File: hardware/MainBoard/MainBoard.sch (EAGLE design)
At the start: 238 parts, among them J1 CON-71741-2184-BOT, J2 CON-71741-2184-TOP, J3 CON-FTSH-105-01-L-DV-K, J4 CON-ZX62R-B-5P, J5 CON-SMA, J6 CON-SMA, J7 CON-RJ45-J0G-0007NL, J8 SWITCH-CJS-1200-1200, M1 MOUNT-HOLE3.3, M2 MOUNT-HOLE3.3, M3 MOUNT-HOLE3.3, M4 MOUNT-HOLE3.3, M5 FIDUCIAL1X2, M6 FIDUCIAL1X2, M7 FIDUCIAL1X2, M8 FIDUCIAL1X2, Q1 MMBT3904, SW1 SWITCH-KSC-201J, SW2 SWITCH-KSC-201J, U1 A2F500M3G-FG256, U2 MAX19706-T4877-4, U3 MAX19706-T4877-4, U4 USBLC6-2SC6, U5 FT232HL, U6 DP83848C-VBH48A, U7 93LC56BT-OT, U8 DS1818-10-SOT-23, U9 LMV112, X1 FOX924B, X2 ECX-31B, X3 ASEM1-C, X5 ECX-42-120

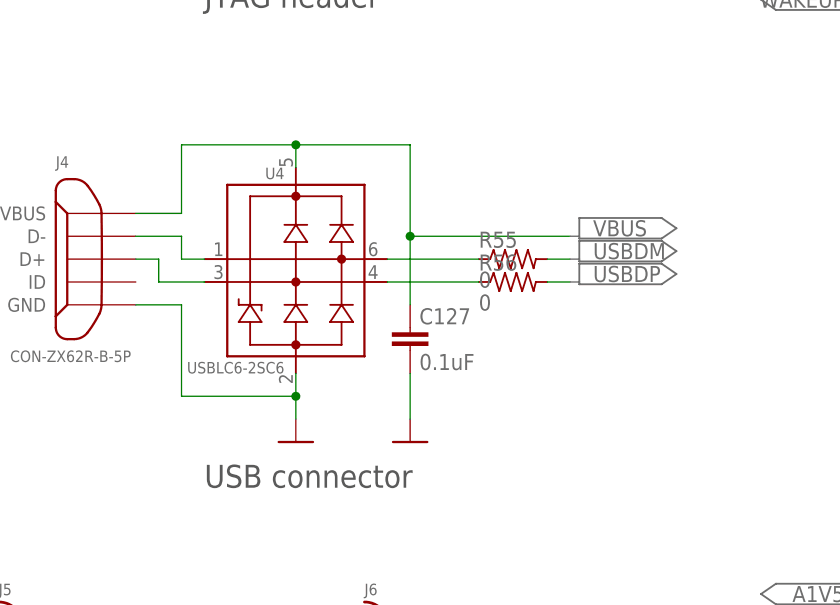
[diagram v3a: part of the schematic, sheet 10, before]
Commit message: Minor corrections in MainBoard library and board.
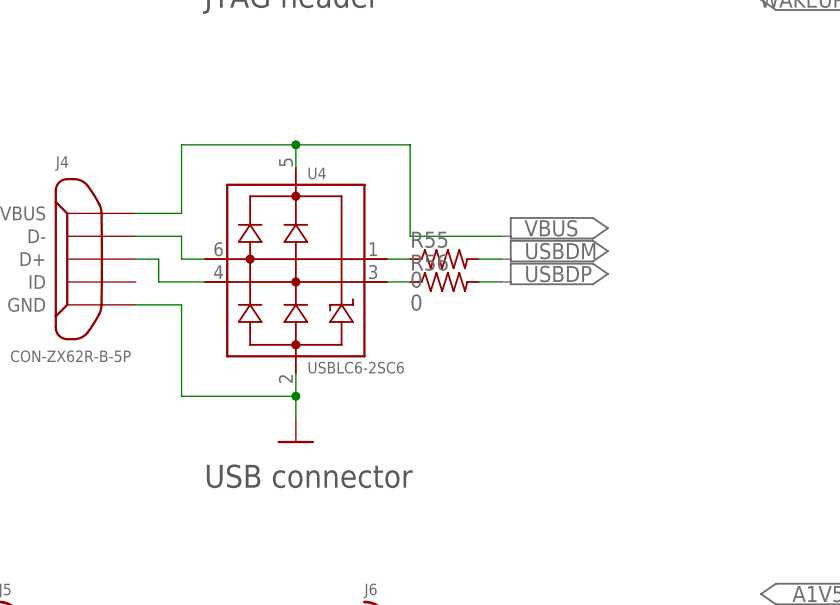
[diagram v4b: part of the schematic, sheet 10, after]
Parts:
- removed C127: 0.1uF, MainBoard:C0402
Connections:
- removed net USBDP-OUT: R56.1, U4.IO2@2
- new net N$26: R56.1, U4.IO2@1
- net DGND: no longer C127.2
- net USBDM-IN: now also U4.IO1@2; no longer U4.IO1@1
- net USBDM-OUT: now also U4.IO1@1; no longer U4.IO1@2
- net USBDP-IN: now also U4.IO2@2; no longer U4.IO2@1
- net VBUS: no longer C127.1
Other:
- note removed: "Place close to USBLC6 output"
- moved on the sheet: R55, R56
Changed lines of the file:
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@@
 <part name="C125" library="MainBoard" deviceset="C" device="0402"/>
 <part name="C126" library="MainBoard" deviceset="C" device="0402"/>
-<part name="C127" library="MainBoard" deviceset="C" device="0402" value="0.1uF"/>
-<part name="U$143" library="MainBoard" deviceset="DGND" device=""/>
 </parts>
 <sheets>
@@
 <instance part="R96" gate="G$1" x="101.6" y="119.38"/>
 <instance part="PORT258" gate="G$1" x="154.94" y="71.12" rot="R90"/>
-<instance part="PORT259" gate="G$1" x="190.5" y="78.74" rot="R90"/>
+<instance part="PORT259" gate="G$1" x="190.5" y="83.82" rot="R90"/>
 <instance part="PORT260" gate="G$1" x="53.34" y="73.66" rot="R90"/>
 <instance part="B2" gate="G$1" x="60.96" y="60.96" rot="R90"/>
@@
 <rectangle x1="60.96" y1="55.88" x2="96.52" y2="68.58" layer="116"/>
 <rectangle x1="17.78" y1="17.78" x2="104.14" y2="30.48" layer="116"/>
-<text x="73.66" y="88.9" size="1.778" layer="150" rot="R90">Place close to USBLC6 output</text>
 </plain>
 <instances>
@@
 <instance part="J6" gate="G1" x="66.04" y="60.96"/>
 <instance part="J4" gate="G$1" x="35.56" y="101.6" rot="MR0"/>
-<instance part="U4" gate="G$1" x="55.88" y="101.6" rot="MR0"/>
+<instance part="U4" gate="G$1" x="55.88" y="101.6"/>
 <instance part="U$13" gate="G$1" x="165.1" y="149.86"/>
 <instance part="PORT15" gate="G$1" x="175.26" y="160.02" rot="MR0"/>
@@
 <instance part="J1" gate="G$1" x="134.62" y="114.3"/>
 <instance part="U$68" gate="G$1" x="55.88" y="81.28"/>
-<instance part="R55" gate="G$1" x="81.28" y="101.6"/>
-<instance part="R56" gate="G$1" x="81.28" y="99.06"/>
-<instance part="PORT172" gate="G$1" x="96.52" y="104.14"/>
-<instance part="PORT173" gate="G$1" x="96.52" y="101.6"/>
-<instance part="PORT174" gate="G$1" x="96.52" y="99.06"/>
+<instance part="R55" gate="G$1" x="73.66" y="101.6"/>
+<instance part="R56" gate="G$1" x="73.66" y="99.06"/>
+<instance part="PORT172" gate="G$1" x="88.9" y="104.14"/>
+<instance part="PORT173" gate="G$1" x="88.9" y="101.6"/>
+<instance part="PORT174" gate="G$1" x="88.9" y="99.06"/>
 <instance part="U$83" gate="G$1" x="71.12" y="137.16"/>
 <instance part="PORT201" gate="G$1" x="30.48" y="152.4" rot="MR0"/>
@@
 <instance part="PORT351" gate="G$1" x="104.14" y="134.62" rot="MR0"/>
 <instance part="PORT352" gate="G$1" x="104.14" y="137.16" rot="MR0"/>
-<instance part="C127" gate="G$1" x="68.58" y="93.98"/>
-<instance part="U$143" gate="G$1" x="68.58" y="81.28"/>
 </instances>
 <busses>
@@
 <junction x="71.12" y="142.24"/>
 </segment>
-<segment>
-<pinref part="C127" gate="G$1" pin="2"/>
-<wire x1="68.58" y1="88.9" x2="68.58" y2="83.82" width="0.1524" layer="91"/>
-<pinref part="U$143" gate="G$1" pin="DGND"/>
-</segment>
 </net>
 <net name="A1V5" class="0">
@@
 <wire x1="38.1" y1="104.14" x2="43.18" y2="104.14" width="0.1524" layer="91"/>
 <wire x1="43.18" y1="104.14" x2="43.18" y2="101.6" width="0.1524" layer="91"/>
-<pinref part="U4" gate="G$1" pin="IO1@1"/>
+<pinref part="U4" gate="G$1" pin="IO1@2"/>
 <wire x1="43.18" y1="101.6" x2="45.72" y2="101.6" width="0.1524" layer="91"/>
 </segment>
@@
 <wire x1="38.1" y1="101.6" x2="40.64" y2="101.6" width="0.1524" layer="91"/>
 <wire x1="40.64" y1="101.6" x2="40.64" y2="99.06" width="0.1524" layer="91"/>
-<pinref part="U4" gate="G$1" pin="IO2@1"/>
+<pinref part="U4" gate="G$1" pin="IO2@2"/>
 <wire x1="40.64" y1="99.06" x2="45.72" y2="99.06" width="0.1524" layer="91"/>
 </segment>
@@
 <net name="VBUS" class="0">
 <segment>
-<label x="88.9" y="104.14" size="1.778" layer="97"/>
-<wire x1="86.36" y1="104.14" x2="68.58" y2="104.14" width="0.1524" layer="91"/>
+<label x="81.28" y="104.14" size="1.778" layer="97"/>
+<wire x1="78.74" y1="104.14" x2="68.58" y2="104.14" width="0.1524" layer="91"/>
 <pinref part="J4" gate="G$1" pin="VBUS"/>
 <wire x1="38.1" y1="106.68" x2="43.18" y2="106.68" width="0.1524" layer="91"/>
@@
 <wire x1="68.58" y1="104.14" x2="68.58" y2="114.3" width="0.1524" layer="91"/>
 <wire x1="68.58" y1="114.3" x2="55.88" y2="114.3" width="0.1524" layer="91"/>
-<pinref part="C127" gate="G$1" pin="1"/>
-<wire x1="68.58" y1="96.52" x2="68.58" y2="104.14" width="0.1524" layer="91"/>
-<junction x="68.58" y="104.14"/>
 </segment>
 </net>
 <net name="USBDM-OUT" class="0">
 <segment>
+<pinref part="U4" gate="G$1" pin="IO1@1"/>
 <pinref part="R55" gate="G$1" pin="1"/>
-<pinref part="U4" gate="G$1" pin="IO1@2"/>
-<wire x1="76.2" y1="101.6" x2="66.04" y2="101.6" width="0.1524" layer="91"/>
+<wire x1="66.04" y1="101.6" x2="68.58" y2="101.6" width="0.1524" layer="91"/>
 </segment>
 </net>
-<net name="USBDP-OUT" class="0">
+<net name="N$26" class="0">
 <segment>
+<pinref part="U4" gate="G$1" pin="IO2@1"/>
 <pinref part="R56" gate="G$1" pin="1"/>
-<pinref part="U4" gate="G$1" pin="IO2@2"/>
-<wire x1="76.2" y1="99.06" x2="66.04" y2="99.06" width="0.1524" layer="91"/>
+<wire x1="66.04" y1="99.06" x2="68.58" y2="99.06" width="0.1524" layer="91"/>
 </segment>
 </net>
@@
 <segment>
 <pinref part="R55" gate="G$1" pin="2"/>
-<wire x1="83.82" y1="101.6" x2="86.36" y2="101.6" width="0.1524" layer="91"/>
-<label x="88.9" y="101.6" size="1.778" layer="97"/>
+<wire x1="76.2" y1="101.6" x2="78.74" y2="101.6" width="0.1524" layer="91"/>
+<label x="81.28" y="101.6" size="1.778" layer="97"/>
 </segment>
 </net>
@@
 <segment>
 <pinref part="R56" gate="G$1" pin="2"/>
-<wire x1="83.82" y1="99.06" x2="86.36" y2="99.06" width="0.1524" layer="91"/>
-<label x="88.9" y="99.06" size="1.778" layer="97"/>
+<wire x1="76.2" y1="99.06" x2="78.74" y2="99.06" width="0.1524" layer="91"/>
+<label x="81.28" y="99.06" size="1.778" layer="97"/>
 </segment>
 </net>

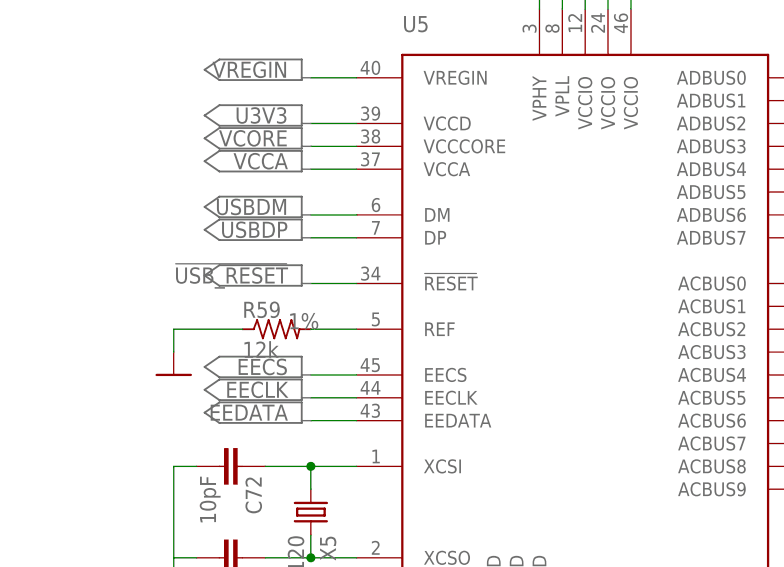
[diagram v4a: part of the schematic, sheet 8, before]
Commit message: Still checking and adjusting USB related components on board.
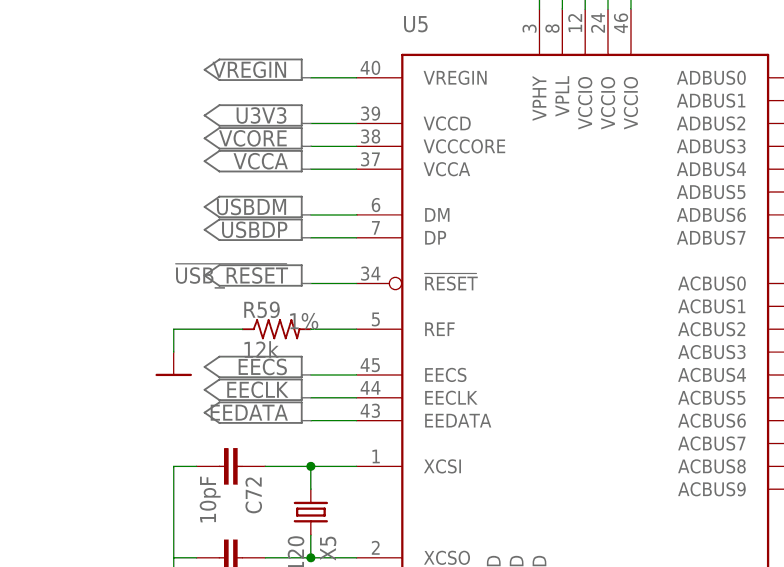
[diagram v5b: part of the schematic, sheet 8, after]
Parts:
- X5: CLOAD (none) -> 9 pF
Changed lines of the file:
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@@
 <part name="U$74" library="MainBoard" deviceset="DGND" device=""/>
 <part name="U$75" library="MainBoard" deviceset="DGND" device=""/>
-<part name="X5" library="MainBoard" deviceset="ECX-42" device="" technology="-120"/>
+<part name="X5" library="MainBoard" deviceset="ECX-42" device="" technology="-120">
+<attribute name="CLOAD" value="9 pF"/>
+</part>
 <part name="C71" library="MainBoard" deviceset="C" device="0402" value="10pF"/>
 <part name="C72" library="MainBoard" deviceset="C" device="0402" value="10pF"/>

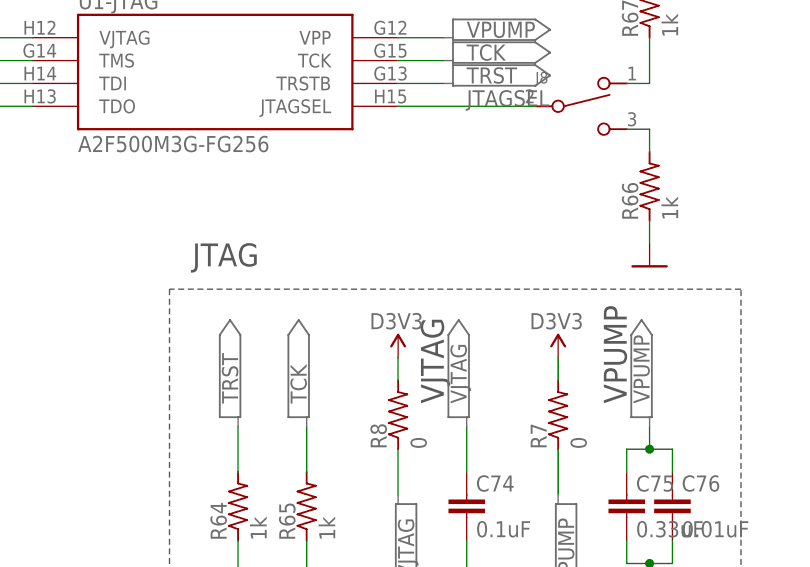
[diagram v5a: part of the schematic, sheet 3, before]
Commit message: Initial checking of USB related parts (almost) finished.
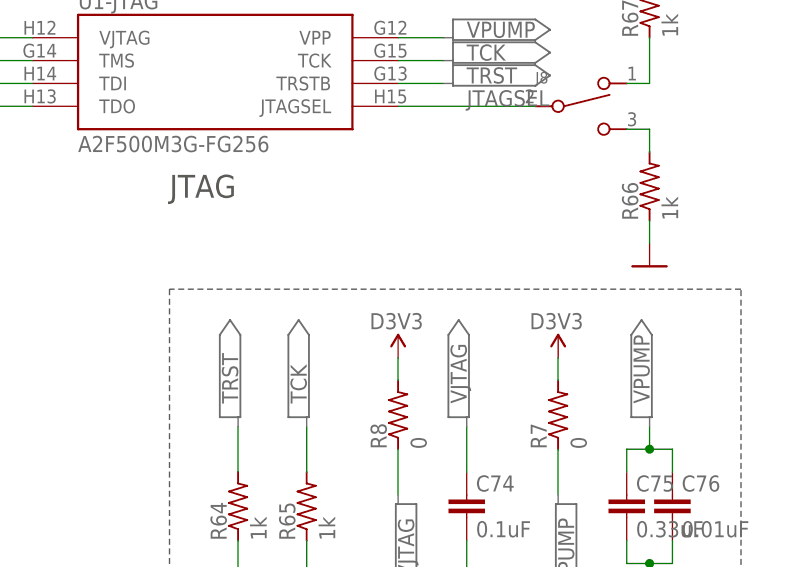
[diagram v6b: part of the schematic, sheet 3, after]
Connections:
- net N$23 renamed UREF
- net N$26 renamed USBDP-OUT
- net N$53 renamed EEDO
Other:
- note added: "RXD"
- note added: "TXD"
- note removed: "VJTAG"
- note removed: "VPUMP"
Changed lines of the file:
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@@
 <text x="50.8" y="104.14" size="50.8" layer="208">CLK</text>
 <text x="55.88" y="40.64" size="50.8" layer="208">RST</text>
-<text x="170.18" y="81.28" size="2.54" layer="97">JTAG</text>
-<text x="198.12" y="66.04" size="2.54" layer="97" rot="R90">VJTAG</text>
+<text x="167.64" y="88.9" size="2.54" layer="97">JTAG</text>
 <wire x1="167.64" y1="40.64" x2="231.14" y2="40.64" width="0.1524" layer="97" style="shortdash"/>
 <wire x1="231.14" y1="40.64" x2="231.14" y2="78.74" width="0.1524" layer="97" style="shortdash"/>
 <wire x1="231.14" y1="78.74" x2="167.64" y2="78.74" width="0.1524" layer="97" style="shortdash"/>
 <wire x1="167.64" y1="78.74" x2="167.64" y2="40.64" width="0.1524" layer="97" style="shortdash"/>
-<text x="218.44" y="66.04" size="2.54" layer="97" rot="R90">VPUMP</text>
 <text x="106.68" y="12.7" size="1.778" layer="97">NC</text>
 <text x="139.7" y="12.7" size="1.778" layer="97">NC</text>
@@
 <rectangle x1="220.98" y1="127" x2="238.76" y2="132.08" layer="116"/>
 <rectangle x1="218.44" y1="91.44" x2="238.76" y2="93.98" layer="116"/>
+<text x="101.6" y="154.94" size="1.778" layer="97">TXD</text>
+<text x="101.6" y="152.4" size="1.778" layer="97">RXD</text>
 </plain>
 <instances>
@@
 </segment>
 </net>
-<net name="N$23" class="0">
+<net name="UREF" class="0">
 <segment>
 <pinref part="U5" gate="G$1" pin="REF"/>
@@
 </segment>
 </net>
-<net name="N$53" class="0">
+<net name="EEDO" class="0">
 <segment>
 <pinref part="U7" gate="G$1" pin="DO"/>
@@
 </segment>
 </net>
-<net name="N$26" class="0">
+<net name="USBDP-OUT" class="0">
 <segment>
 <pinref part="U4" gate="G$1" pin="IO2@1"/>

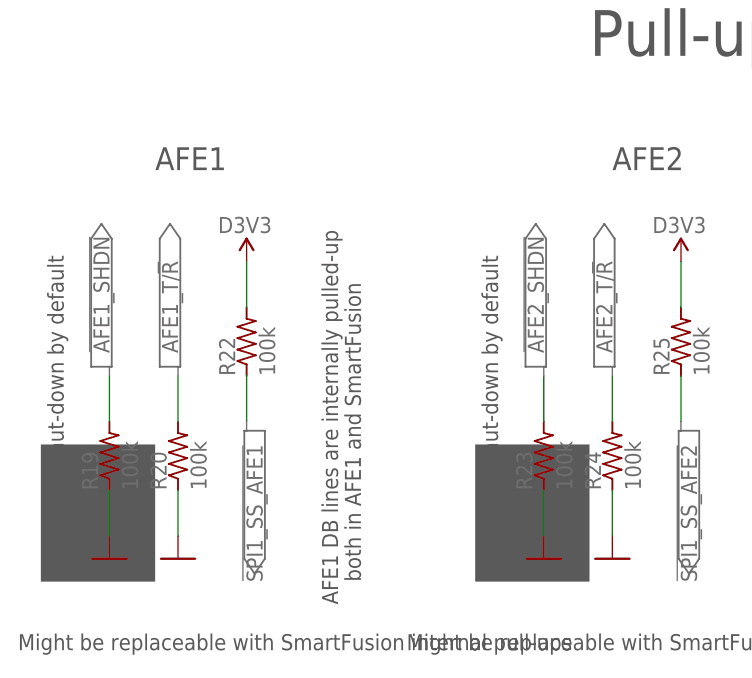
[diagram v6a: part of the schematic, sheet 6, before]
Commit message: Checked EXT AFE power supply and decoupling capacitors.
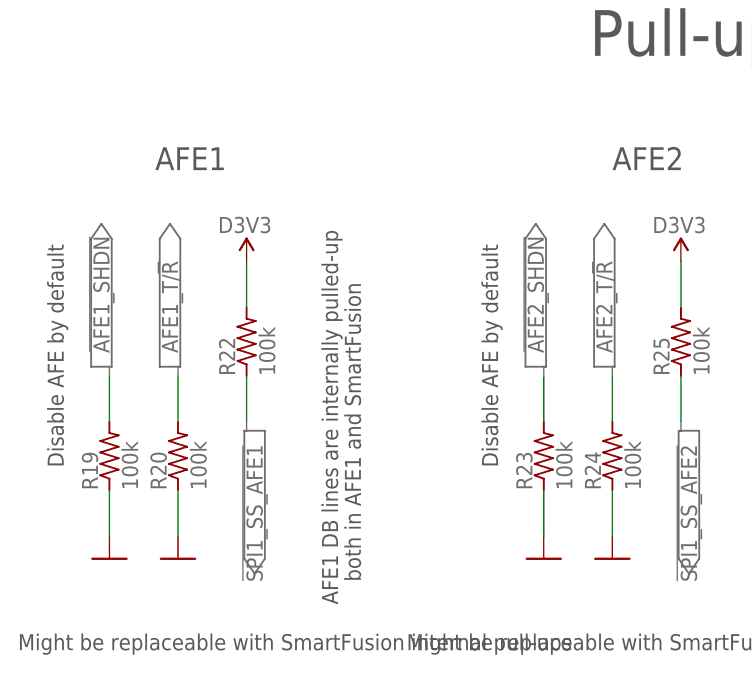
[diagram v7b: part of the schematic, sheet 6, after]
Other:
- note added: "Disable AFE by default"
- note removed: "Shut-down by default"
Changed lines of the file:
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@@
 <text x="142.24" y="157.48" size="2.54" layer="97" rot="R90">VDD</text>
 <text x="200.66" y="157.48" size="2.54" layer="97" rot="R90">OVDD</text>
-<rectangle x1="17.78" y1="17.78" x2="30.48" y2="33.02" layer="97"/>
-<text x="20.32" y="30.48" size="1.778" layer="97" rot="R90">Shut-down by default</text>
+<text x="20.32" y="30.48" size="1.778" layer="97" rot="R90">Disable AFE by default</text>
 <text x="76.2" y="157.48" size="2.54" layer="97" rot="R90">REFIN</text>
 <text x="142.24" y="114.3" size="2.54" layer="97" rot="R90">VDD</text>
 <text x="200.66" y="114.3" size="2.54" layer="97" rot="R90">OVDD</text>
 <text x="76.2" y="114.3" size="2.54" layer="97" rot="R90">REFIN</text>
-<rectangle x1="66.04" y1="17.78" x2="78.74" y2="33.02" layer="97"/>
-<text x="68.58" y="30.48" size="1.778" layer="97" rot="R90">Shut-down by default</text>
 <text x="50.8" y="15.24" size="1.778" layer="97" rot="R90">AFE1 DB lines are internally pulled-up</text>
 <text x="53.34" y="17.78" size="1.778" layer="97" rot="R90">both in AFE1 and SmartFusion</text>
@@
 <rectangle x1="30.48" y1="91.44" x2="203.2" y2="127" layer="116"/>
 <rectangle x1="10.16" y1="15.24" x2="121.92" y2="68.58" layer="116"/>
+<text x="68.58" y="30.48" size="1.778" layer="97" rot="R90">Disable AFE by default</text>
+<rectangle x1="76.2" y1="17.78" x2="86.36" y2="58.42" layer="98"/>
+<rectangle x1="27.94" y1="17.78" x2="38.1" y2="58.42" layer="98"/>
 </plain>
 <instances>
